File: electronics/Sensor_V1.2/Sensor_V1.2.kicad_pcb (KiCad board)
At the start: 2 copper layers, 45.9 x 25.6 mm, 35 parts, among them J1 nuclone_small_left, J2 nuclone_small_right, J3 Proto_1pin, J5 DevBoardUartInput, Q1 DMG1012, U1 PPG_sensor

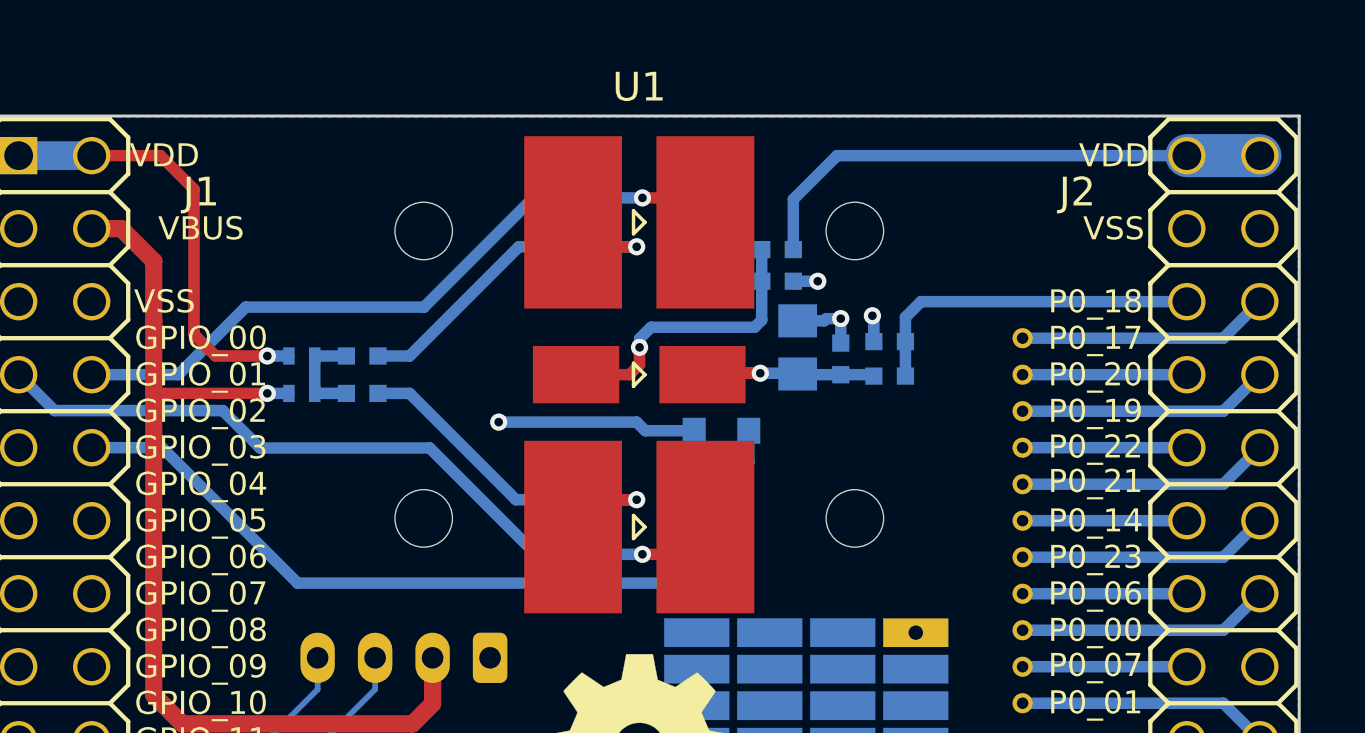
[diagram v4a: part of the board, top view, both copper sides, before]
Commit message: rerouting/re-placement of components
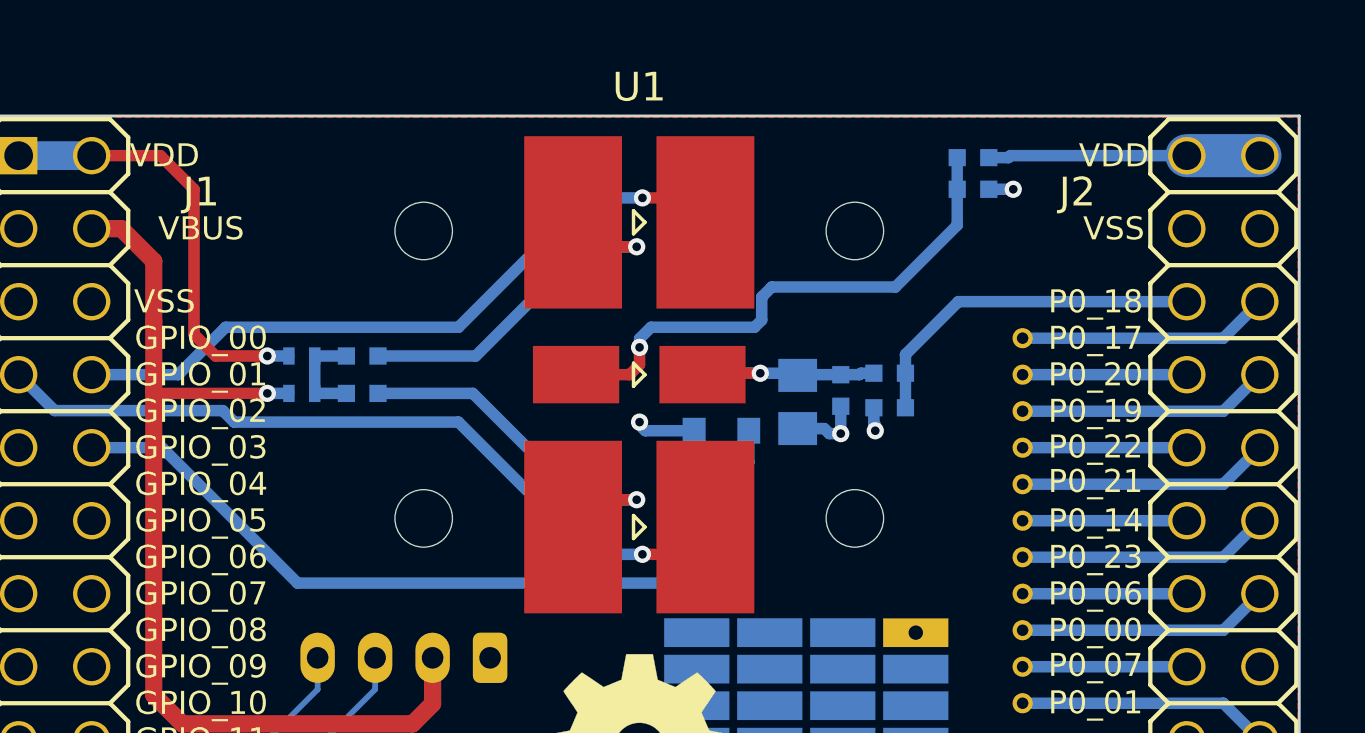
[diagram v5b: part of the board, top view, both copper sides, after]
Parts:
- moved C1 7.52 mm to (96.7, 76.1)
- moved FB3 7.52 mm to (96.7, 75.0)
- moved C2 2.30 mm to (93.8, 83.7)
- moved C9 1.90 mm to (90.6, 83.5), turned to 270 degrees
- moved R3 1.10 mm to (92.1, 83.1), turned to 270 degrees
- moved R4 0.10 mm to (93.8, 82.5)
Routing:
- net /VDDA: track 18.6 -> 9.46 mm
- net /PD_BIAS: track 10.2 -> 18.8 mm
- net /VSS: track 12.5 -> 7.68 mm
